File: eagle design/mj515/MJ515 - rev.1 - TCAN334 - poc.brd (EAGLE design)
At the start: 100 x 34.8 mm, 38 parts, among them IC202 LDK320AM33R, IC302 STM32F042G6U6, IC401 TCAN334, IC501 ADXL345, IC502 74HCT1G32GW

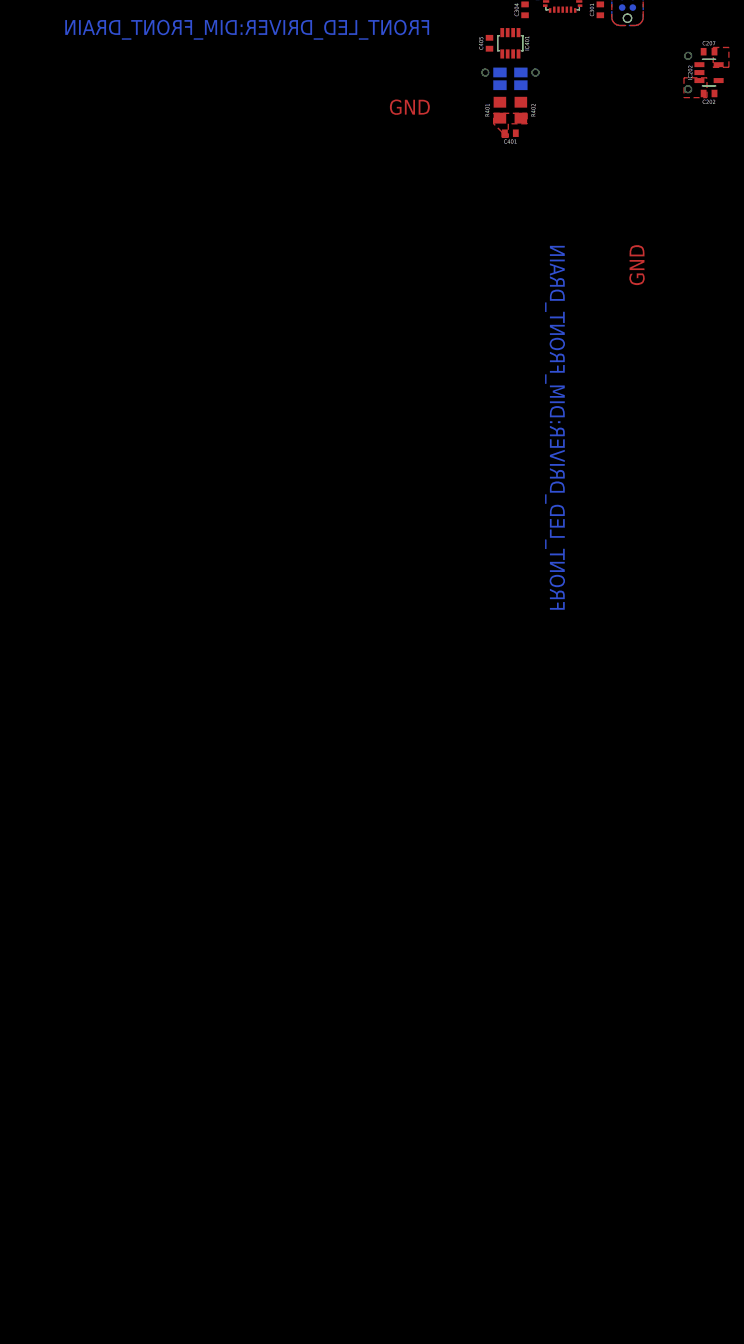
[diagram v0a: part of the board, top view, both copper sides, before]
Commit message: MJ818 SuperNova Mini2: - added position key into PCB and spacers; updated gerber, dwg and stl
mj513 - grip:
- corrected bushing dimensions

in mj8x8-foo:
- minor corrections

general board-wide effort:
- replaced pinhead with 0.9mm TH
- added 2nd CAN H & L solder contact
- unified sch nets and drawings

in mj8x8 foo:
- developed rev.1b mj-foo device with voltage detector and CAN TVS protection

in mj808 design:
- updated front led shunt resistor to 0.18 Ohm

in mj8x8:
- added HR30-6R-6P - PushPull Receptacle.lbr receptable
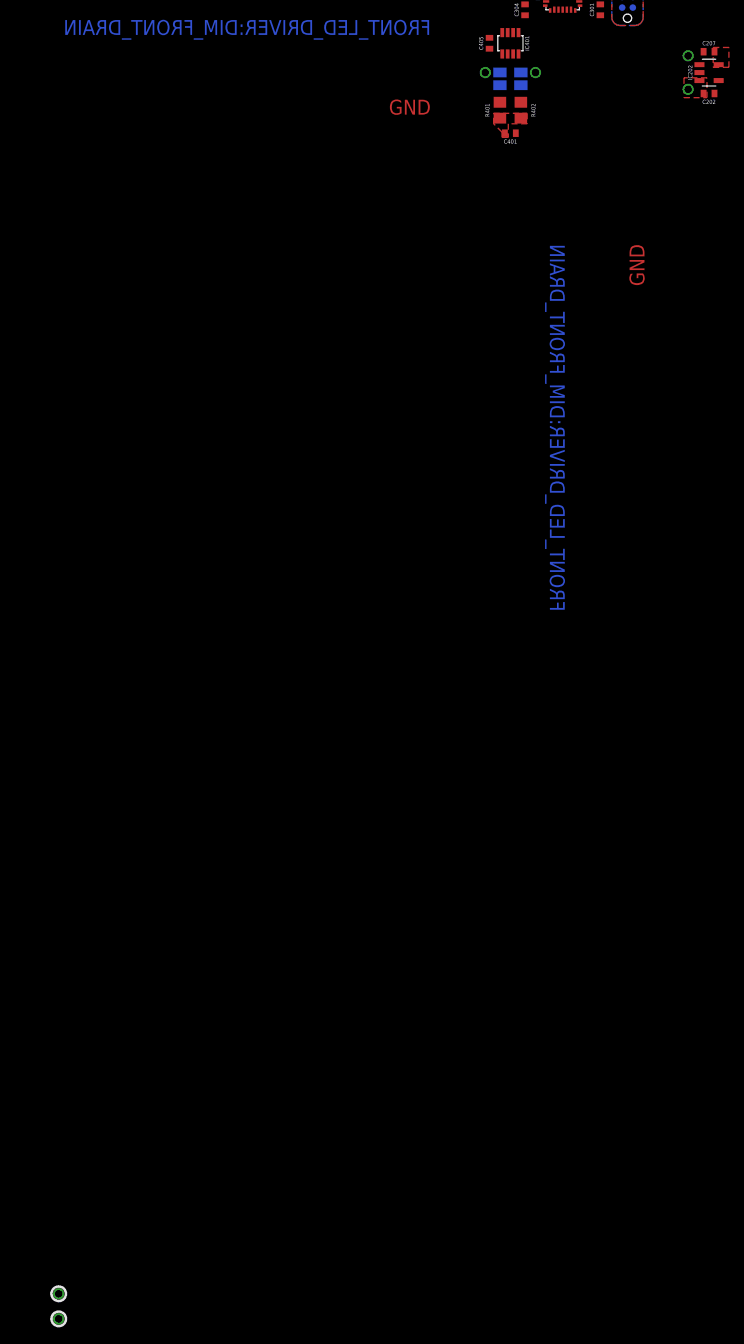
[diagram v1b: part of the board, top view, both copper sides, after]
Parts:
- added TP3: CAN high, signal testpoint:TH-0.9
- added TP4: CAN low, signal testpoint:TH-0.9
- TP1, TP2, TP5, TP6: device signal testpoint:TH-0.6 -> signal testpoint:TH-0.9
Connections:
- net BAT+: now also TP1.P$1; no longer TP1.TP$1
- net CAN_H: now also TP3.P$1, TP5.P$1; no longer TP5.TP$1
- net CAN_L: now also TP4.P$1, TP6.P$1; no longer TP6.TP$1
- net GND: now also TP2.P$1; no longer TP2.TP$1
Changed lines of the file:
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@@
 <layer number="19" name="Unrouted" color="6" fill="1" visible="yes" active="yes"/>
 <layer number="20" name="Dimension" color="24" fill="1" visible="yes" active="yes"/>
-<layer number="21" name="tPlace" color="7" fill="1" visible="no" active="yes"/>
+<layer number="21" name="tPlace" color="7" fill="1" visible="yes" active="yes"/>
 <layer number="22" name="bPlace" color="7" fill="1" visible="no" active="yes"/>
 <layer number="23" name="tOrigins" color="15" fill="1" visible="yes" active="yes"/>
@@
 <layer number="45" name="Holes" color="7" fill="1" visible="no" active="yes"/>
 <layer number="46" name="Milling" color="3" fill="1" visible="yes" active="yes"/>
-<layer number="47" name="Measures" color="7" fill="1" visible="yes" active="yes"/>
+<layer number="47" name="Measures" color="7" fill="1" visible="no" active="yes"/>
 <layer number="48" name="Document" color="7" fill="1" visible="no" active="yes"/>
 <layer number="49" name="Reference" color="7" fill="1" visible="no" active="yes"/>
@@
 </autorouter>
 <elements>
-<element name="TP2" library="signal testpoint" package="TH-0.6" value="LiIon - Terminal" x="-99.75" y="52" smashed="yes" rot="MR90"/>
-<element name="TP5" library="signal testpoint" package="TH-0.6" value="CAN high" x="-118" y="50" smashed="yes" rot="MR0"/>
-<element name="TP6" library="signal testpoint" package="TH-0.6" value="CAN low" x="-124" y="50" smashed="yes" rot="MR0"/>
-<element name="TP1" library="signal testpoint" package="TH-0.6" value="LiIon + Terminal" x="-99.75" y="48" smashed="yes" rot="MR90"/>
+<element name="TP2" library="signal testpoint" package="TH-0.9" value="LiIon - Terminal" x="-99.75" y="52" smashed="yes" rot="MR90"/>
+<element name="TP5" library="signal testpoint" package="TH-0.9" value="CAN high" x="-118" y="50" smashed="yes" rot="MR0"/>
+<element name="TP6" library="signal testpoint" package="TH-0.9" value="CAN low" x="-124" y="50" smashed="yes" rot="MR0"/>
+<element name="TP1" library="signal testpoint" package="TH-0.9" value="LiIon + Terminal" x="-99.75" y="48" smashed="yes" rot="MR90"/>
 <element name="SWD1" library="tag-connect" package="TC2030-NL" value="TC2030-NL" x="-107" y="56.5" smashed="yes" rot="MR90">
 <attribute name="VALUE" x="-107" y="62.5" size="0.5" layer="28" font="vector" rot="MR180" align="center"/>
@@
 <attribute name="VALUE" x="45.635" y="3.58" size="1.27" layer="27" rot="R180"/>
 </element>
+<element name="TP3" library="signal testpoint" package="TH-0.9" value="CAN high" x="-175" y="-96" smashed="yes"/>
+<element name="TP4" library="signal testpoint" package="TH-0.9" value="CAN low" x="-175" y="-99" smashed="yes"/>
 </elements>
 <signals>
 <signal name="GND">
-<contactref element="TP2" pad="TP$1"/>
+<contactref element="TP2" pad="P$1"/>
 <contactref element="IC302" pad="16_VSS"/>
 <contactref element="C202" pad="2"/>
@@
 <wire x1="-120.35" y1="42.75" x2="-123.5" y2="52.85" width="0" layer="19" extent="1-1"/>
 <wire x1="45.5" y1="1.675" x2="-62.6" y2="-74.4" width="0" layer="19" extent="1-1"/>
+<wire x1="45.5" y1="3.675" x2="45.5" y2="1.675" width="0" layer="19" extent="1-1"/>
+<wire x1="45.5" y1="5.675" x2="45.5" y2="3.675" width="0" layer="19" extent="1-1"/>
+<wire x1="45.5" y1="7.675" x2="45.5" y2="5.675" width="0" layer="19" extent="1-1"/>
+<wire x1="45.5" y1="9.675" x2="45.5" y2="7.675" width="0" layer="19" extent="1-1"/>
 </signal>
 <signal name="BAT+" class="4">
-<contactref element="TP1" pad="TP$1"/>
+<contactref element="TP1" pad="P$1"/>
 <contactref element="IC202" pad="EN"/>
 <contactref element="IC202" pad="IN"/>
@@
 <vertex x="-97.5" y="49.375"/>
 </polygon>
-<wire x1="-98.4" y1="49.046" x2="-98.4" y2="50.946" width="0" layer="19" extent="1-1"/>
+<wire x1="-98.4" y1="49.046" x2="-99.75" y2="48" width="0" layer="19" extent="1-1"/>
+<wire x1="-97.9" y1="47.5" x2="-98.4" y2="49.046" width="0" layer="19" extent="1-1"/>
+<wire x1="-98.4" y1="50.946" x2="-98.4" y2="49.046" width="0" layer="19" extent="1-1"/>
 </signal>
 <signal name="CAN_H" class="3">
-<contactref element="TP5" pad="TP$1"/>
+<contactref element="TP5" pad="P$1"/>
 <contactref element="IC401" pad="P$7"/>
 <contactref element="SJ401" pad="1"/>
+<contactref element="TP3" pad="P$1"/>
 <wire x1="-118" y1="50" x2="-119.75" y2="50.012" width="0" layer="19" extent="16-16"/>
 <wire x1="-120.675" y1="52.225" x2="-119.75" y2="50.012" width="0" layer="19" extent="1-16"/>
+<wire x1="-175" y1="-96" x2="-119.75" y2="50.012" width="0" layer="19" extent="16-16"/>
 </signal>
 <signal name="CAN_L" class="3">
-<contactref element="TP6" pad="TP$1"/>
+<contactref element="TP6" pad="P$1"/>
 <contactref element="IC401" pad="P$6"/>
 <contactref element="SJ402" pad="1"/>
+<contactref element="TP4" pad="P$1"/>
 <wire x1="-122.25" y1="50.012" x2="-124" y2="50" width="0" layer="19" extent="16-16"/>
 <wire x1="-121.325" y1="52.225" x2="-122.25" y2="50.012" width="0" layer="19" extent="1-16"/>
+<wire x1="-175" y1="-99" x2="-124" y2="50" width="0" layer="19" extent="1-1"/>
 </signal>
 <signal name="3V3" class="2">
@@
 <wire x1="39.15" y1="9.675" x2="39.15" y2="7.675" width="0" layer="19" extent="1-1"/>
 <wire x1="-96.1" y1="50.946" x2="-63.9" y2="-72.6" width="0" layer="19" extent="1-1"/>
+<wire x1="-96.6" y1="52.492" x2="-96.1" y2="50.946" width="0" layer="19" extent="1-1"/>
 <wire x1="-107.635" y1="57.77" x2="-96.6" y2="52.492" width="0" layer="19" extent="1-16"/>
 <wire x1="-110.25" y1="58.15" x2="-107.635" y2="57.77" width="0" layer="19" extent="1-16"/>
@@
 <contactref element="IC501" pad="INT2"/>
 </signal>
-<signal name="MISO" class="4">
+<signal name="MISO" class="3">
 <contactref element="IC501" pad="SDO"/>
 <contactref element="IC302" pad="12_PA6"/>
 <wire x1="-114.25" y1="57.52" x2="-57.95" y2="-84.05" width="0" layer="19" extent="1-1"/>
 </signal>
-<signal name="MOSI" class="4">
+<signal name="MOSI" class="3">
 <contactref element="IC502" pad="B"/>
 <contactref element="IC302" pad="13_PA7"/>
 <wire x1="-113.75" y1="57.52" x2="-63.9" y2="-74.4" width="0" layer="19" extent="1-1"/>
 </signal>
-<signal name="CLK" class="4">
+<signal name="CLK" class="3">
 <contactref element="IC501" pad="SCL"/>
 <contactref element="IC302" pad="11_PA5"/>
 <wire x1="-114.75" y1="57.52" x2="-59.25" y2="-82.95" width="0" layer="19" extent="1-1"/>
 </signal>
-<signal name="CS" class="4">
+<signal name="CS" class="3">
 <contactref element="IC501" pad="!CS!"/>
 <contactref element="IC502" pad="A"/>
@@
 <wire x1="-115.25" y1="57.52" x2="-63.25" y2="-74.4" width="0" layer="19" extent="1-1"/>
 </signal>
-<signal name="ADXL345_INT1" class="4">
+<signal name="ADXL345_INT1" class="3">
 <contactref element="IC501" pad="INT1"/>
 <contactref element="IC302" pad="6_PA0"/>
 <wire x1="-116.73" y1="58.5" x2="-57.95" y2="-87.25" width="0" layer="19" extent="1-1"/>
 </signal>
-<signal name="BIT4" class="4">
+<signal name="BIT4" class="3">
 <contactref element="IC302" pad="27_PB6"/>
 <contactref element="R605" pad="2"/>
@@
 <wire x1="44.5" y1="1.675" x2="40.85" y2="1.675" width="0" layer="19" extent="1-1"/>
 </signal>
-<signal name="BIT1" class="4">
+<signal name="BIT1" class="3">
 <contactref element="IC302" pad="24_PB3"/>
 <contactref element="R602" pad="2"/>
@@
 <wire x1="44.5" y1="7.675" x2="40.85" y2="7.675" width="0" layer="19" extent="1-1"/>
 </signal>
-<signal name="BIT2" class="4">
+<signal name="BIT2" class="3">
 <contactref element="IC302" pad="25_PB4"/>
 <contactref element="R603" pad="2"/>
@@
 <wire x1="44.5" y1="5.675" x2="40.85" y2="5.675" width="0" layer="19" extent="1-1"/>
 </signal>
-<signal name="BIT3" class="4">
+<signal name="BIT3" class="3">
 <contactref element="IC302" pad="26_PB5"/>
 <contactref element="R604" pad="2"/>
@@
 <wire x1="44.5" y1="3.675" x2="40.85" y2="3.675" width="0" layer="19" extent="1-1"/>
 </signal>
-<signal name="IDX" class="4">
+<signal name="IDX" class="3">
 <contactref element="IC302" pad="7_PA1"/>
 <contactref element="LED606" pad="E"/>
